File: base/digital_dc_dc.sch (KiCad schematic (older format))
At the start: 34 parts, among them U14 AMS1117-5.0, U15 AMS1117-5.0, U16 LM2596S-ADJ

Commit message: upd
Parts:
- renumbered C22 to C20, C23 to C21, C24 to C22, C25 to C23, C26 to C24, C27 to C25, C28 to C26, C29 to C27, C30 to C28, C31 to C29, C32 to C30, C33 to C31, C34 to C32, C35 to C33
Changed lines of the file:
@@
 $EndComp
 $Comp
-L C C24
+L C C22
 U 1 1 5A393804
 P 2800 3250
-F 0 "C24" H 2825 3350 50  0000 L CNN
+F 0 "C22" H 2825 3350 50  0000 L CNN
 F 1 "3.3nF 50V" H 2825 3150 50  0000 L CNN
 F 2 "Capacitor_SMD:C_0603_1608Metric" H 2838 3100 50  0001 C CNN
@@
 $EndComp
 $Comp
-L CP C25
+L CP C23
 U 1 1 5A393B3D
 P 3400 3250
-F 0 "C25" H 3425 3350 50  0000 L CNN
+F 0 "C23" H 3425 3350 50  0000 L CNN
 F 1 "220uF 35V" H 3425 3150 50  0000 L CNN
 F 2 "Capacitor_SMD:CP_Elec_8x10" H 3438 3100 50  0001 C CNN
@@
 $EndComp
 $Comp
-L CP C30
+L CP C28
 U 1 1 5A394320
 P 4500 3250
-F 0 "C30" H 4525 3350 50  0000 L CNN
+F 0 "C28" H 4525 3350 50  0000 L CNN
 F 1 "220uF 35V" H 4525 3150 50  0000 L CNN
 F 2 "Capacitor_SMD:CP_Elec_8x10" H 4538 3100 50  0001 C CNN
@@
 $EndComp
 $Comp
-L C C31
+L C C29
 U 1 1 5A394607
 P 5100 3250
-F 0 "C31" H 5125 3350 50  0000 L CNN
+F 0 "C29" H 5125 3350 50  0000 L CNN
 F 1 "4.7uF 50V" H 5125 3150 50  0000 L CNN
 F 2 "Capacitor_SMD:C_1210_3225Metric" H 5138 3100 50  0001 C CNN
@@
 $EndComp
 $Comp
-L C C32
+L C C30
 U 1 1 5A394844
 P 5800 3250
-F 0 "C32" H 5825 3350 50  0000 L CNN
+F 0 "C30" H 5825 3350 50  0000 L CNN
 F 1 "4.7uF 50V" H 5825 3150 50  0000 L CNN
 F 2 "Capacitor_SMD:C_1210_3225Metric" H 5838 3100 50  0001 C CNN
@@
 $EndComp
 $Comp
-L CP C33
+L CP C31
 U 1 1 5A3964F4
 P 8300 3450
-F 0 "C33" H 8325 3550 50  0000 L CNN
+F 0 "C31" H 8325 3550 50  0000 L CNN
 F 1 "470uF 10V" H 8325 3350 50  0000 L CNN
 F 2 "Capacitor_SMD:CP_Elec_8x10" H 8338 3300 50  0001 C CNN
@@
 $EndComp
 $Comp
-L C C35
+L C C33
 U 1 1 5A396963
 P 10050 3450
-F 0 "C35" H 10075 3550 50  0000 L CNN
+F 0 "C33" H 10075 3550 50  0000 L CNN
 F 1 "0.1uF" H 10075 3350 50  0000 L CNN
 F 2 "Capacitor_SMD:C_0603_1608Metric" H 10088 3300 50  0001 C CNN
@@
 +6.8V
 $Comp
-L CP C22
+L CP C20
 U 1 1 5A3971EB
 P 2500 4550
-F 0 "C22" H 2525 4650 50  0000 L CNN
+F 0 "C20" H 2525 4650 50  0000 L CNN
 F 1 "22uF 10V" H 2525 4450 50  0000 L CNN
 F 2 "Capacitor_Tantalum_SMD:CP_EIA-3216-18_Kemet-A" H 2538 4400 50  0001 C CNN
@@
 $EndComp
 $Comp
-L CP C26
+L CP C24
 U 1 1 5A3988D5
 P 3500 4550
-F 0 "C26" H 3525 4650 50  0000 L CNN
+F 0 "C24" H 3525 4650 50  0000 L CNN
 F 1 "22uF 6.3V" H 3525 4450 50  0000 L CNN
 F 2 "Capacitor_Tantalum_SMD:CP_EIA-3216-18_Kemet-A" H 3538 4400 50  0001 C CNN
@@
 $EndComp
 $Comp
-L C C28
+L C C26
 U 1 1 5A398AEE
 P 4100 4550
-F 0 "C28" H 4125 4650 50  0000 L CNN
+F 0 "C26" H 4125 4650 50  0000 L CNN
 F 1 "4.7uF 6.3V" H 4125 4450 50  0000 L CNN
 F 2 "Capacitor_SMD:C_0603_1608Metric" H 4138 4400 50  0001 C CNN
@@
 $EndComp
 $Comp
-L CP C23
+L CP C21
 U 1 1 5A398DF8
 P 2500 5600
-F 0 "C23" H 2525 5700 50  0000 L CNN
+F 0 "C21" H 2525 5700 50  0000 L CNN
 F 1 "22uF 10V" H 2525 5500 50  0000 L CNN
 F 2 "Capacitor_Tantalum_SMD:CP_EIA-3216-18_Kemet-A" H 2538 5450 50  0001 C CNN
@@
 $EndComp
 $Comp
-L CP C27
+L CP C25
 U 1 1 5A398E13
 P 3500 5600
-F 0 "C27" H 3525 5700 50  0000 L CNN
+F 0 "C25" H 3525 5700 50  0000 L CNN
 F 1 "22uF 6.3V" H 3525 5500 50  0000 L CNN
 F 2 "Capacitor_Tantalum_SMD:CP_EIA-3216-18_Kemet-A" H 3538 5450 50  0001 C CNN
@@
 $EndComp
 $Comp
-L C C29
+L C C27
 U 1 1 5A398E1E
 P 4100 5600
-F 0 "C29" H 4125 5700 50  0000 L CNN
+F 0 "C27" H 4125 5700 50  0000 L CNN
 F 1 "4.7uF 6.3V" H 4125 5500 50  0000 L CNN
 F 2 "Capacitor_SMD:C_0603_1608Metric" H 4138 5450 50  0001 C CNN
@@
 $EndComp
 $Comp
-L CP C34
+L CP C32
 U 1 1 5A3A1070
 P 9000 3450
-F 0 "C34" H 9025 3550 50  0000 L CNN
+F 0 "C32" H 9025 3550 50  0000 L CNN
 F 1 "470uF 10V" H 9025 3350 50  0000 L CNN
 F 2 "Capacitor_SMD:CP_Elec_8x10" H 9038 3300 50  0001 C CNN

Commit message: current version
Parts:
- removed TP30: +24Vd_IN, TestPoint:TestPoint_Pad_D1.5mm, symbol Test_Point
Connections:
- wire segments 67 -> 66
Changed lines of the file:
@@
 	4250 5250 4250 5350
 Connection ~ 4250 5350
-$Comp
-L Test_Point TP30
-U 1 1 5A4A0D23
-P 1300 2700
-F 0 "TP30" H 1300 2970 50  0000 C CNN
-F 1 "+24Vd_IN" H 1300 2900 50  0000 C CNN
-F 2 "TestPoint:TestPoint_Pad_D1.5mm" H 1500 2700 50  0001 C CNN
-F 3 "" H 1500 2700 50  0001 C CNN
-	1    1300 2700
-	1    0    0    -1
-$EndComp
-Wire Wire Line
-	1300 2700 1300 3000
 Connection ~ 1300 3000
 $Comp

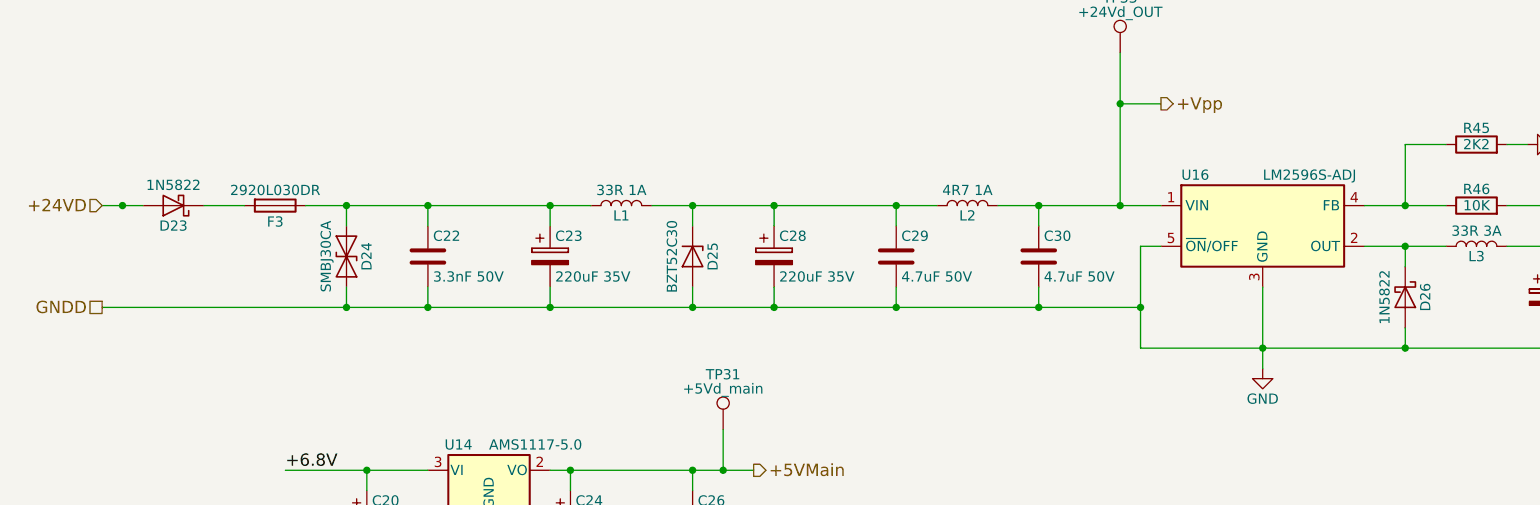
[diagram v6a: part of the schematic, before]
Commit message: edit reference for diodes in digital_dc_dc
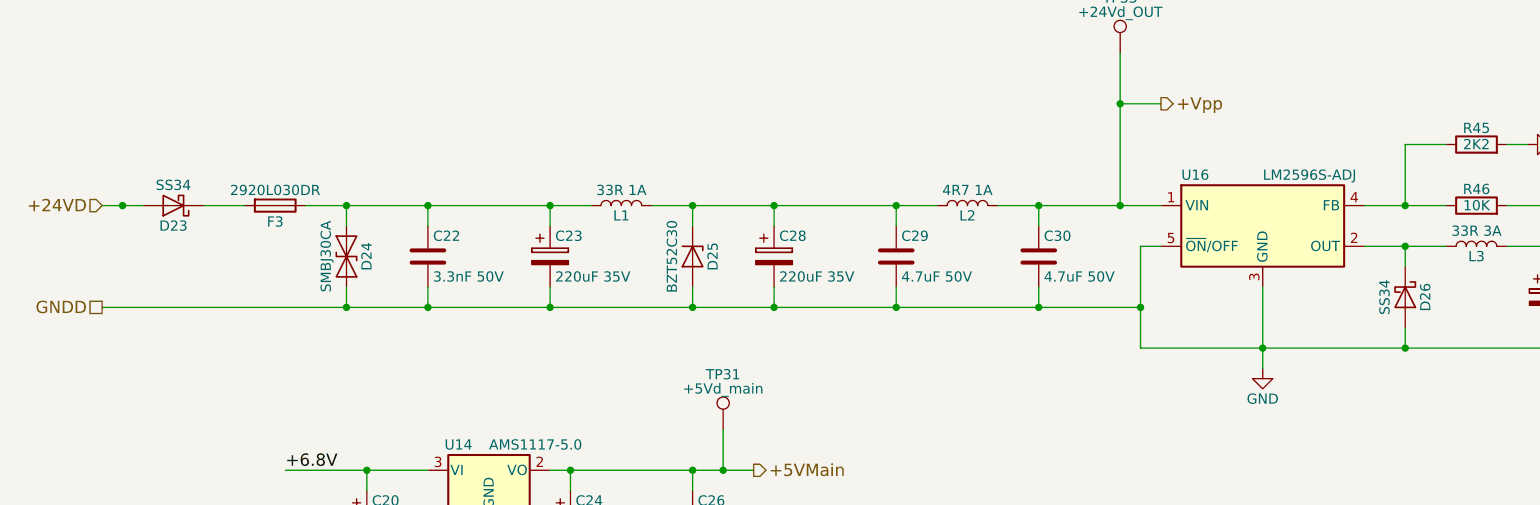
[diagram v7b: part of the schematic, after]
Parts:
- D23, D26: value 1N5822 -> SS34
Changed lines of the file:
@@
 P 1550 3000
 F 0 "D23" H 1550 3100 50  0000 C CNN
-F 1 "1N5822" H 1550 2900 50  0000 C CNN
+F 1 "SS34" H 1550 2900 50  0000 C CNN
 F 2 "Diode_SMD:D_SMA" H 1550 2825 50  0001 C CNN
 F 3 "" H 1550 3000 50  0001 C CNN
@@
 P 7600 3450
 F 0 "D26" H 7600 3550 50  0000 C CNN
-F 1 "1N5822" H 7600 3350 50  0000 C CNN
+F 1 "SS34" H 7600 3350 50  0000 C CNN
 F 2 "Diode_SMD:D_SMA" H 7600 3275 50  0001 C CNN
 F 3 "" H 7600 3450 50  0001 C CNN
